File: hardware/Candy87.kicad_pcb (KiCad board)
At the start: 2 copper layers, 343.6 x 123.4 mm, 247 parts, among them J1 ai03_ud, J2 USB_C_Receptacle_USB2.0, J3 Conn_01x07_Pin, U1 RP2040, U2 AMS1117-3.3, U3 W25Q128JVS, U4 USBLC6-2SC6, U5 74AHCT1G125, Y1 12MHz

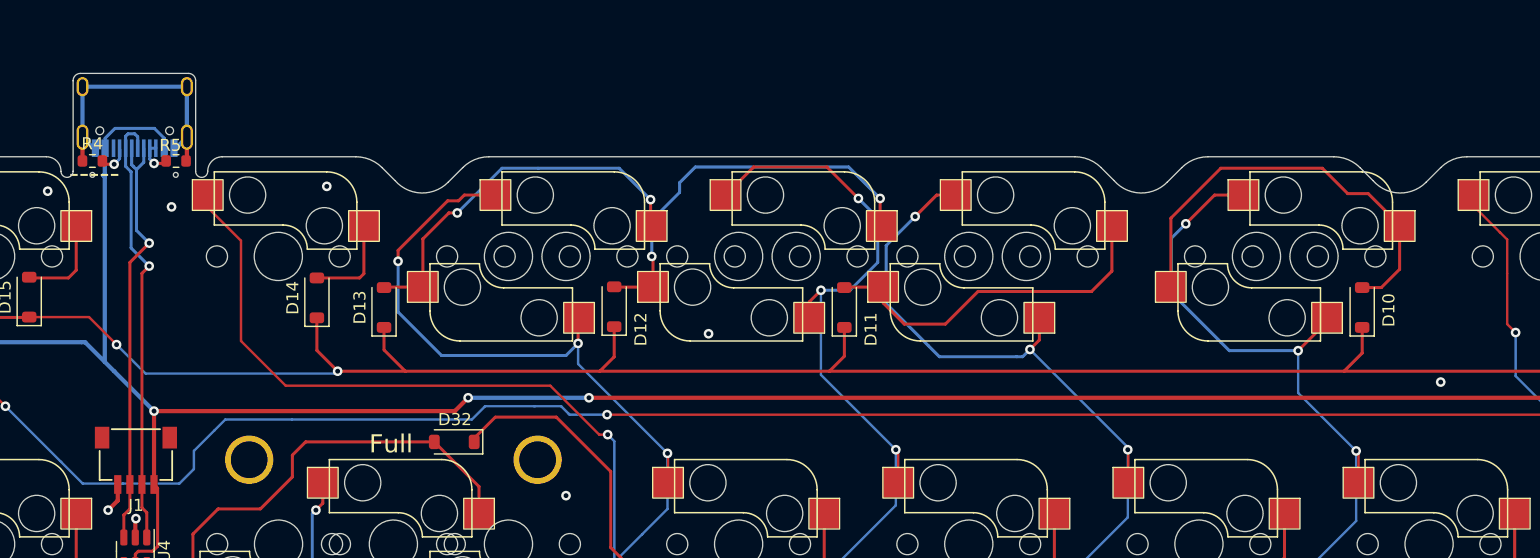
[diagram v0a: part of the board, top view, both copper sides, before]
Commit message: Minor changes
Minimal changes to USB Port:
- Removed wrong line from CC2 to A8 on USB-C
- A tiny tiny bit bigger PCB Edge around USB Port

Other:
- Added/changed Logos

New gerbers, cpl/bom stay the same (no changes)
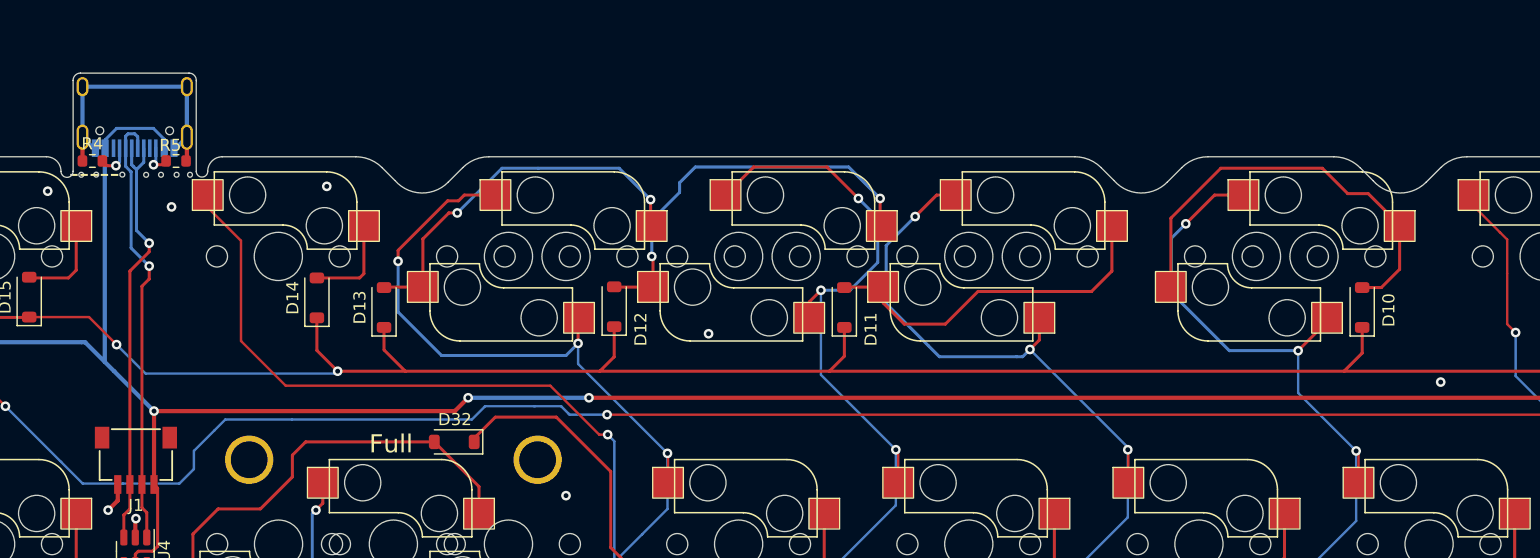
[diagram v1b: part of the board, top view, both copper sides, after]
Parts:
- removed the Ref** at (217.9, -40.5)
- added ?: , , F.Cu at (36.7, -146.0)
- added ?: , , F.Cu at (32.6, -146.0)
- added ?: , , F.Cu at (40.3, -146.0)
- added ?: , , F.Cu at (34.7, -146.0)
- added ?: , , F.Cu at (37.9, -146.0)
- added G***: LOGO, LOGO, B.Cu at (218.0, -40.2)
- added G***: LOGO, LOGO, B.Cu at (14.6, -74.8)
- added Ref**: Val**, CK:candy87-5, B.Cu at (14.4, -82.5)
- moved ? 0.92 mm to (31.3, -146.0)
- moved ? 0.07 mm to (39.2, -146.0)
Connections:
- J2 pad A8: Net-(J2-CC2) -> unconnected-(J2-SBU1-PadA8)
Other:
- board size 343.6 x 123.4 mm -> 343.6 x 123.5 mm
